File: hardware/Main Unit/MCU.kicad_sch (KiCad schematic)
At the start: 36 parts, among them J1 3221-10-0300-00, SW1 MJTP1243, SW2 MJTP1243, U1 MCXN547VKLT, X1 24.0000MHz

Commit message: Implement Ethernet, start on voltage regulator
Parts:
- J1: footprint ProjectLibrary:3221-10-0300-00 -> Project Library:3221-10-0300-00
- R2, R23, R3, R4: LibRef (none) -> RC0603FR-0710KL
- U1: footprint Package_QFP:LQFP-100-1EP_14x14mm_P0.5mm_EP6.9x6.9mm -> Project Library:LQFP-100-1EP_14x14mm_P0.5mm_EP6.9x6.9mm_Fixed3DModel
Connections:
- net DBG_UART.MCU_RX: now reaches U1.35 (P4_12)
- net DBG_UART.MCU_TX: now reaches U1.36 (P4_13)
- net ~{ETH_SPEED_LED}: now reaches U1.48 (P5_0)
- net ~{SD_CARD_EN}: now reaches U1.49 (P5_1)
- no-connect marks 5 -> 7
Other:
- moved on the sheet: U1F
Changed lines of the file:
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@@
 	)
 	(no_connect
+		(at 168.91 426.72)
+	)
+	(no_connect
 		(at 60.96 257.81)
 	)
@@
 	)
 	(no_connect
+		(at 168.91 424.18)
+	)
+	(no_connect
 		(at 127 223.52)
 	)
@@
 	)
 	(bus_entry
+		(at 306.07 506.73)
+		(size 2.54 -2.54)
+		(stroke
+			(width 0)
+			(type default)
+		)
+	)
+	(bus_entry
 		(at 241.3 111.76)
 		(size 2.54 -2.54)
@@
 	)
 	(bus_entry
+		(at 306.07 510.54)
+		(size 2.54 -2.54)
+		(stroke
+			(width 0)
+			(type default)
+		)
+	)
+	(bus_entry
 		(at 299.72 339.09)
 		(size 2.54 -2.54)
@@
 		)
 	)
+	(bus
+		(pts
+			(xy 306.07 510.54) (xy 306.07 518.16)
+		)
+		(stroke
+			(width 0)
+			(type default)
+		)
+	)
 	(wire
 		(pts
@@
 		)
 	)
+	(bus
+		(pts
+			(xy 283.21 518.16) (xy 306.07 518.16)
+		)
+		(stroke
+			(width 0)
+			(type default)
+		)
+	)
 	(wire
 		(pts
@@
 	(bus
 		(pts
+			(xy 306.07 506.73) (xy 306.07 510.54)
+		)
+		(stroke
+			(width 0)
+			(type default)
+		)
+	)
+	(bus
+		(pts
 			(xy 313.69 292.1) (xy 313.69 295.91)
 		)
@@
 	(wire
 		(pts
+			(xy 308.61 504.19) (xy 349.25 504.19)
+		)
+		(stroke
+			(width 0)
+			(type default)
+		)
+	)
+	(wire
+		(pts
 			(xy 92.71 252.73) (xy 92.71 229.87)
 		)
@@
 	(bus
 		(pts
+			(xy 306.07 502.92) (xy 306.07 506.73)
+		)
+		(stroke
+			(width 0)
+			(type default)
+		)
+	)
+	(bus
+		(pts
 			(xy 368.3 393.7) (xy 325.12 393.7)
 		)
@@
 	(wire
 		(pts
+			(xy 323.85 529.59) (xy 349.25 529.59)
+		)
+		(stroke
+			(width 0)
+			(type default)
+		)
+	)
+	(wire
+		(pts
 			(xy 85.09 130.81) (xy 74.93 130.81)
 		)
@@
 	(wire
 		(pts
+			(xy 308.61 508) (xy 349.25 508)
+		)
+		(stroke
+			(width 0)
+			(type default)
+		)
+	)
+	(wire
+		(pts
 			(xy 95.25 201.93) (xy 88.9 201.93)
 		)
@@
 	(wire
 		(pts
+			(xy 323.85 533.4) (xy 349.25 533.4)
+		)
+		(stroke
+			(width 0)
+			(type default)
+		)
+	)
+	(wire
+		(pts
 			(xy 146.05 66.04) (xy 154.94 66.04)
 		)
@@
 		)
 	)
+	(label "DBG_UART.MCU_RX"
+		(at 347.98 504.19 180)
+		(effects
+			(font
+				(size 1.27 1.27)
+			)
+			(justify right bottom)
+		)
+	)
 	(label "CARD_SPI_FC8.~{CS}0"
 		(at 327.66 374.65 0)
@@
 		)
 	)
+	(label "DBG_UART.MCU_TX"
+		(at 347.98 508 180)
+		(effects
+			(font
+				(size 1.27 1.27)
+			)
+			(justify right bottom)
+		)
+	)
 	(label "uSD_SPI_FC6.MISO"
 		(at 273.05 347.98 0)
@@
 	)
 	(hierarchical_label "~{RST}"
-		(shape output)
+		(shape bidirectional)
 		(at 72.39 189.23 180)
 		(effects
@@
 		)
 	)
+	(hierarchical_label "~{ETH_SPEED_LED}"
+		(shape output)
+		(at 323.85 529.59 180)
+		(effects
+			(font
+				(size 1.27 1.27)
+			)
+			(justify right)
+		)
+	)
 	(hierarchical_label "CARD_SPI_FC7{MOSI MISO SCLK ~{CS}0 ~{CS}1 ~{CS}2 CARD_SEL ~{DRDY}}"
 		(shape bidirectional)
@@
 		)
 	)
+	(hierarchical_label "~{SD_CARD_EN}"
+		(shape output)
+		(at 323.85 533.4 180)
+		(effects
+			(font
+				(size 1.27 1.27)
+			)
+			(justify right)
+		)
+	)
 	(hierarchical_label "CARD_SPI_FC4{MOSI MISO SCLK ~{CS}0 ~{CS}1 ~{CS}2 CARD_SEL ~{DRDY}}"
 		(shape bidirectional)
@@
 		)
 	)
+	(hierarchical_label "DBG_UART{MCU_TX MCU_RX}"
+		(shape bidirectional)
+		(at 283.21 518.16 180)
+		(effects
+			(font
+				(size 1.27 1.27)
+			)
+			(justify right)
+		)
+	)
 	(hierarchical_label "CARD_SPI_FC9{MOSI MISO SCLK ~{CS}0 ~{CS}1 ~{CS}2 CARD_SEL ~{DRDY}}"
 		(shape bidirectional)
@@
 		(on_board yes)
 		(dnp no)
-		(fields_autoplaced yes)
 		(property "Reference" "U1"
-			(at 439.42 505.1844 0)
+			(at 352.298 461.518 0)
 			(effects
 				(font
@@
 		)
 		(property "Value" "MCXN547VKLT"
-			(at 439.42 507.7244 0)
+			(at 352.298 464.058 0)
 			(effects
 				(font
@@
 			)
 		)
-		(property "Footprint" "Package_QFP:LQFP-100-1EP_14x14mm_P0.5mm_EP6.9x6.9mm"
+		(property "Footprint" "Project Library:LQFP-100-1EP_14x14mm_P0.5mm_EP6.9x6.9mm_Fixed3DModel"
 			(at 362.966 611.632 0)
 			(effects
@@
 			)
 		)
-		(property "Footprint" "Package_QFP:LQFP-100-1EP_14x14mm_P0.5mm_EP6.9x6.9mm"
+		(property "Footprint" "Project Library:LQFP-100-1EP_14x14mm_P0.5mm_EP6.9x6.9mm_Fixed3DModel"
 			(at 366.776 428.752 0)
 			(effects
@@
 			)
 		)
-		(property "Description" "Resistor 10k 1% 0.1W 0603"
+		(property "Description" "Resistor, small US symbol"
 			(at 83.82 262.89 0)
 			(effects
@@
 			)
 		)
+		(property "LibRef" "RC0603FR-0710KL"
+			(at 83.82 262.89 0)
+			(effects
+				(font
+					(size 1.27 1.27)
+				)
+				(hide yes)
+			)
+		)
 		(pin "2"
 		)
@@
 			)
 		)
-		(property "Description" "Resistor 10k 1% 0.1W 0603"
+		(property "Description" "Resistor, small US symbol"
 			(at 83.82 246.38 0)
 			(effects
@@
 			)
 		)
+		(property "LibRef" "RC0603FR-0710KL"
+			(at 83.82 246.38 0)
+			(effects
+				(font
+					(size 1.27 1.27)
+				)
+				(hide yes)
+			)
+		)
 		(pin "2"
 		)
@@
 			)
 		)
-		(property "Description" "Resistor 10k 1% 0.1W 0603"
+		(property "Description" "Resistor, small US symbol"
 			(at 92.71 269.24 0)
 			(effects
@@
 			)
 		)
+		(property "LibRef" "RC0603FR-0710KL"
+			(at 92.71 269.24 0)
+			(effects
+				(font
+					(size 1.27 1.27)
+				)
+				(hide yes)
+			)
+		)
 		(pin "2"
 		)
@@
 			)
 		)
-		(property "Footprint" "ProjectLibrary:3221-10-0300-00"
+		(property "Footprint" "Project Library:3221-10-0300-00"
 			(at 46.228 234.95 0)
 			(effects
@@
 			)
 		)
-		(property "Footprint" "Package_QFP:LQFP-100-1EP_14x14mm_P0.5mm_EP6.9x6.9mm"
+		(property "Footprint" "Project Library:LQFP-100-1EP_14x14mm_P0.5mm_EP6.9x6.9mm_Fixed3DModel"
 			(at 362.966 341.122 0)
 			(effects
@@
 			)
 		)
-		(property "Footprint" "Package_QFP:LQFP-100-1EP_14x14mm_P0.5mm_EP6.9x6.9mm"
+		(property "Footprint" "Project Library:LQFP-100-1EP_14x14mm_P0.5mm_EP6.9x6.9mm_Fixed3DModel"
 			(at 358.14 149.86 0)
 			(effects
@@
 			)
 		)
-		(property "Footprint" "Package_QFP:LQFP-100-1EP_14x14mm_P0.5mm_EP6.9x6.9mm"
+		(property "Footprint" "Project Library:LQFP-100-1EP_14x14mm_P0.5mm_EP6.9x6.9mm_Fixed3DModel"
 			(at 110.49 156.21 0)
 			(effects
@@
 			)
 		)
-		(property "Footprint" "Package_QFP:LQFP-100-1EP_14x14mm_P0.5mm_EP6.9x6.9mm"
+		(property "Footprint" "Project Library:LQFP-100-1EP_14x14mm_P0.5mm_EP6.9x6.9mm_Fixed3DModel"
 			(at 143.51 335.28 0)
 			(effects
@@
 	(symbol
 		(lib_id "Project Library:MCXN547VKLT")
-		(at 146.05 340.36 0)
+		(at 195.58 415.29 0)
 		(unit 6)
 		(exclude_from_sim no)
@@
 		(dnp no)
 		(property "Reference" "U1"
-			(at 121.666 322.58 0)
+			(at 171.196 397.51 0)
 			(effects
 				(font
@@
 		)
 		(property "Value" "MCXN547VKLT"
-			(at 121.666 325.12 0)
+			(at 171.196 400.05 0)
 			(effects
 				(font
@@
 			)
 		)
-		(property "Footprint" "Package_QFP:LQFP-100-1EP_14x14mm_P0.5mm_EP6.9x6.9mm"
-			(at 133.096 473.202 0)
+		(property "Footprint" "Project Library:LQFP-100-1EP_14x14mm_P0.5mm_EP6.9x6.9mm_Fixed3DModel"
+			(at 182.626 548.132 0)
 			(effects
 				(font
@@
 		)
 		(property "Datasheet" "https://www.mouser.com/datasheet/3/118/1/MCXNx4xDS.pdf"
-			(at 143.51 470.662 0)
+			(at 193.04 545.592 0)
 			(effects
 				(font
@@
 		)
 		(property "Description" "MCU ARM Cortex-M33 Dual Core, 150MHz, 512kiB RAM, 2MiB Flash"
-			(at 145.288 468.63 0)
+			(at 194.818 543.56 0)
 			(effects
 				(font
@@
 			)
 		)
-		(property "Description" "Resistor 10k 1% 0.1W 0603"
+		(property "Description" "Resistor, small US symbol"
 			(at 82.55 180.34 0)
 			(effects
@@
 			(at 82.55 180.34 0)
 			(effects
+				(font
+					(size 1.27 1.27)
+				)
+				(hide yes)
+			)
+		)
+		(property "LibRef" "RC0603FR-0710KL"
+			(at 82.55 180.34 0)
+			(effects

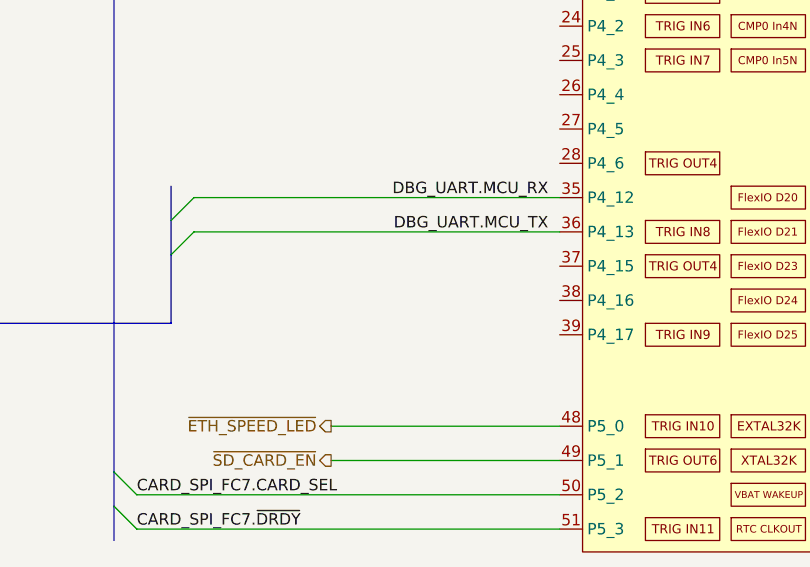
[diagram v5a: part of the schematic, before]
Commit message: Finish 3.3V regulator
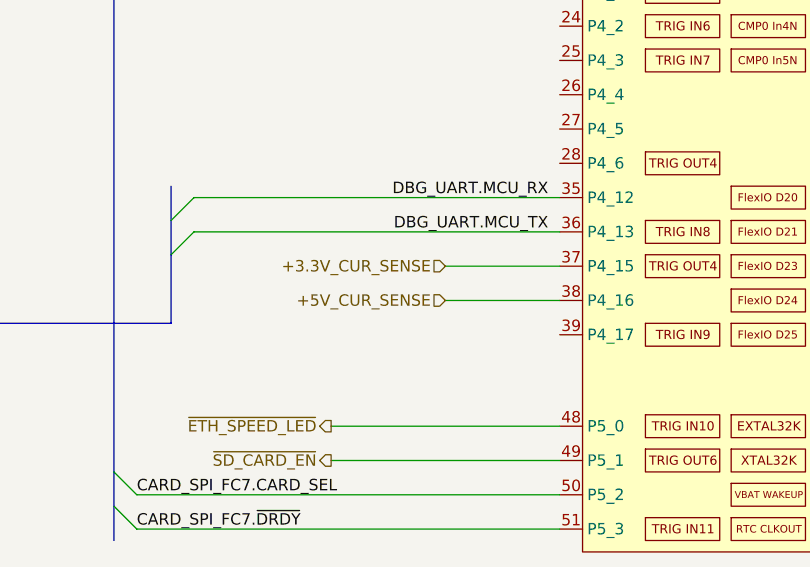
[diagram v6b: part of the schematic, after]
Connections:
- net +3.3V_CUR_SENSE: now reaches U1.37 (P4_15)
- net +5V_CUR_SENSE: now reaches U1.38 (P4_16)
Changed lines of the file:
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@@
 	(wire
 		(pts
+			(xy 336.55 515.62) (xy 349.25 515.62)
+		)
+		(stroke
+			(width 0)
+			(type default)
+		)
+	)
+	(wire
+		(pts
 			(xy 95.25 232.41) (xy 127 232.41)
 		)
@@
 		)
 	)
+	(wire
+		(pts
+			(xy 336.55 511.81) (xy 349.25 511.81)
+		)
+		(stroke
+			(width 0)
+			(type default)
+		)
+	)
 	(bus
 		(pts
@@
 		)
 	)
+	(hierarchical_label "+5V_CUR_SENSE"
+		(shape input)
+		(at 336.55 515.62 180)
+		(effects
+			(font
+				(size 1.27 1.27)
+			)
+			(justify right)
+		)
+	)
 	(hierarchical_label "~{SD_CARD_EN}"
 		(shape output)
@@
 		(effects
 			(font
+				(size 1.27 1.27)
+			)
+			(justify right)
+		)
+	)
+	(hierarchical_label "+3.3V_CUR_SENSE"
+		(shape input)
+		(at 336.55 511.81 180)
+		(effects
+			(font

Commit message: Main unit: Add USB port for MCU and 3.3VA rail, start on routing
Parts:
- added J12: USB4105-GF-A, Project Library:USB_C_Receptacle_GCT_USB4105-xx-A_16P_TopMnt_Horizontal-ExtraHoleClearance, symbol Connector:USB_C_Receptacle_USB2.0_16P
- added R41, R42: 5.1k, Resistor_SMD:R_0603_1608Metric, symbol Device:R_Small_US
- added U13: USBLC6-2SC6, Package_TO_SOT_SMD:SOT-23-6, symbol Power_Protection:USBLC6-2SC6
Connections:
- net +3.3V: no longer C10.1, C11.1, U1.34 (VDD_P4)
- net +3.3VA: now also C10.1, C11.1, U1.34 (VDD_P4)
- net GND: now also J12.A1 (GND), J12.A12 (GND), J12.B1 (GND), J12.B12 (GND), R41.1, R42.1, U13.2 (GND)
- net ~{CARD_SYNC}: now reaches U1.27 (P4_5)
- net ~{CARD_RST}: now reaches U1.28 (P4_6)
- net USBMCU_D+: now reaches U1.40 (USB1_DP)
- net USBMCU_D+: now also U13.4 (I/O2)
- net USBMCU_D-: now reaches U1.41 (USB1_DM)
- net USBMCU_D-: now also U13.6 (I/O1)
- net USBMCU_VBUS: now reaches U1.42 (USB1_VBUS)
- net USBMCU_VBUS: now also J12.A4 (VBUS), J12.A9 (VBUS), J12.B4 (VBUS), J12.B9 (VBUS), U13.5 (VBUS)
- new net: J12.A5 (CC1), R41.2
- new net: J12.B5 (CC2), R42.2
- new net PREFILT_USBMCU_D+: J12.A6 (D+), J12.B6 (D+), U13.3 (I/O2)
- new net PREFILT_USBMCU_D-: J12.A7 (D-), J12.B7 (D-), U13.1 (I/O1)
- no-connect marks 7 -> 10
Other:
- moved on the sheet: U1F

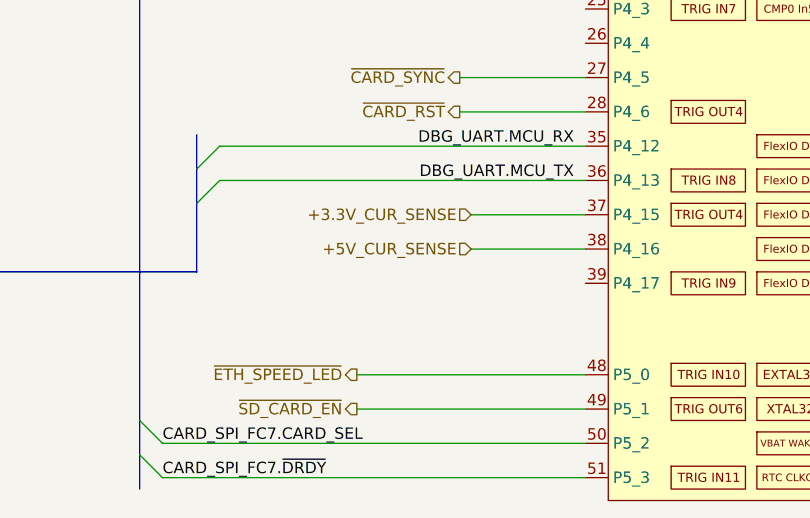
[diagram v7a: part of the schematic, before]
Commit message: Add schematic for Vsupply input
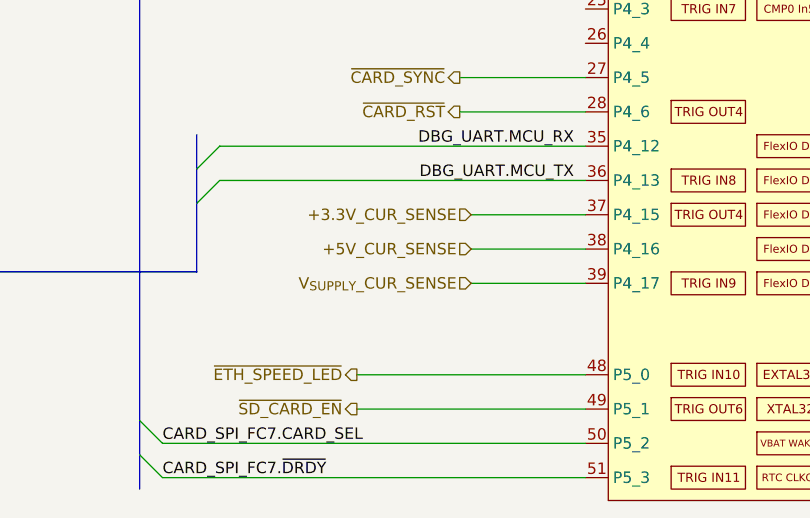
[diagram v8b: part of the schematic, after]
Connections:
- net V_{SUPPLY}_CUR_SENSE: now reaches U1.39 (P4_17)
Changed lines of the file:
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@@
 	(wire
 		(pts
+			(xy 336.55 519.43) (xy 349.25 519.43)
+		)
+		(stroke
+			(width 0)
+			(type default)
+		)
+	)
+	(wire
+		(pts
 			(xy 316.23 309.88) (xy 353.06 309.88)
 		)
@@
 		)
 	)
+	(hierarchical_label "V_{SUPPLY}_CUR_SENSE"
+		(shape input)
+		(at 336.55 519.43 180)
+		(effects
+			(font
+				(size 1.27 1.27)
+			)
+			(justify right)
+		)
+	)
